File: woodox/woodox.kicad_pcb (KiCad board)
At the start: 2 copper layers, 162.2 x 126.5 mm, 0 parts

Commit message: finish left hand pcb
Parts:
- added C10: 1uF, Capacitor_SMD:C_0402_1005Metric, B.Cu at (189.2, 63.3)
- added C11: 1uF, Capacitor_SMD:C_0402_1005Metric, B.Cu at (188.1, 67.5)
- added C12: 10uF, Capacitor_SMD:C_0402_1005Metric, B.Cu at (69.4, 42.3)
- added C13: 0.1uF, Capacitor_SMD:C_0402_1005Metric, B.Cu at (188.8, 68.2)
- added C14: 0.1uF, Capacitor_SMD:C_0402_1005Metric, B.Cu at (183.1, 76.1)
- added C15: 0.1uF, Capacitor_SMD:C_0402_1005Metric, B.Cu at (189.4, 68.8)
- added C16: 0.1uF, Capacitor_SMD:C_0402_1005Metric, B.Cu at (184.1, 76.1)
- added C17: 10uF, Capacitor_SMD:C_0402_1005Metric, B.Cu at (63.8, 37.5)
- added C18: 0.1uF, Capacitor_SMD:C_0402_1005Metric, B.Cu at (185.1, 76.1)
- added C19: 0.1uF, Capacitor_SMD:C_0402_1005Metric, B.Cu at (186.0, 76.1)
- added C20: 0.1uF, Capacitor_SMD:C_0402_1005Metric, B.Cu at (187.0, 76.1)
- added C21: 0.1uF, Capacitor_SMD:C_0402_1005Metric, B.Cu at (188.0, 76.1)
- added C22: 0.1uF, Capacitor_SMD:C_0402_1005Metric, B.Cu at (189.0, 76.1)
- added C23: 1uF, Capacitor_SMD:C_0402_1005Metric, B.Cu at (185.0, 98.5)
- added C24: 0.1uF, Capacitor_SMD:C_0402_1005Metric, B.Cu at (185.7, 97.8)
- added C25: 1uF, Capacitor_SMD:C_0402_1005Metric, B.Cu at (183.7, 99.8)
- added C26: 0.1uF, Capacitor_SMD:C_0402_1005Metric, B.Cu at (184.3, 99.1)
- added C27: 1uF, Capacitor_SMD:C_0402_1005Metric, B.Cu at (182.3, 101.2)
- added C28: 0.1uF, Capacitor_SMD:C_0402_1005Metric, B.Cu at (183.0, 100.5)
- added C7: 0.1uF, Capacitor_SMD:C_0402_1005Metric, B.Cu at (189.2, 72.1)
- added C8: 27pF, Capacitor_SMD:C_0402_1005Metric, B.Cu at (174.8, 64.4)
- added C9: 27pF, Capacitor_SMD:C_0402_1005Metric, B.Cu at (174.8, 57.1)
- added D33: LED_RGB, marbastlib-mx:LED_MX_6028R, B.Cu at (65.3, 49.1)
- added D34: LED_RGB, marbastlib-mx:LED_MX_6028R, B.Cu at (65.3, 68.2)
- added D35: LED_RGB, marbastlib-mx:LED_MX_6028R, B.Cu at (65.3, 87.2)
- added D36: LED_RGB, marbastlib-mx:LED_MX_6028R, B.Cu at (65.3, 106.3)
- added D37: LED_RGB, marbastlib-mx:LED_MX_6028R, B.Cu at (67.8, 125.3)
- added D38: LED_RGB, marbastlib-mx:LED_MX_6028R, B.Cu at (86.9, 49.1)
- added D39: LED_RGB, marbastlib-mx:LED_MX_6028R, B.Cu at (86.9, 68.2)
- added D40: LED_RGB, marbastlib-mx:LED_MX_6028R, B.Cu at (86.9, 87.2)
- added D41: LED_RGB, marbastlib-mx:LED_MX_6028R, B.Cu at (86.9, 106.3)
- added D42: LED_RGB, marbastlib-mx:LED_MX_6028R, B.Cu at (105.9, 44.7)
- added D43: LED_RGB, marbastlib-mx:LED_MX_6028R, B.Cu at (105.9, 63.7)
- added D44: LED_RGB, marbastlib-mx:LED_MX_6028R, B.Cu at (105.9, 82.8)
- added D45: LED_RGB, marbastlib-mx:LED_MX_6028R, B.Cu at (105.9, 101.8)
- added D46: LED_RGB, marbastlib-mx:LED_MX_6028R, B.Cu at (105.7, 120.9)
- added D47: LED_RGB, marbastlib-mx:LED_MX_6028R, B.Cu at (125.0, 42.1)
- added D48: LED_RGB, marbastlib-mx:LED_MX_6028R, B.Cu at (125.0, 61.2)
- added D49: LED_RGB, marbastlib-mx:LED_MX_6028R, B.Cu at (125.0, 80.2)
- added D50: LED_RGB, marbastlib-mx:LED_MX_6028R, B.Cu at (125.0, 99.3)
- added D51: LED_RGB, marbastlib-mx:LED_MX_6028R, B.Cu at (124.7, 118.3)
- added D52: LED_RGB, marbastlib-mx:LED_MX_6028R, B.Cu at (144.0, 44.7)
- added D53: LED_RGB, marbastlib-mx:LED_MX_6028R, B.Cu at (144.0, 63.7)
- added D54: LED_RGB, marbastlib-mx:LED_MX_6028R, B.Cu at (144.0, 82.8)
- added D55: LED_RGB, marbastlib-mx:LED_MX_6028R, B.Cu at (144.0, 101.8)
- added D56: LED_RGB, marbastlib-mx:LED_MX_6028R, B.Cu at (151.5, 124.2)
- added D57: LED_RGB, marbastlib-mx:LED_MX_6028R, B.Cu at (163.1, 46.6)
- added D58: LED_RGB, marbastlib-mx:LED_MX_6028R, B.Cu at (163.1, 65.6)
- added D59: LED_RGB, marbastlib-mx:LED_MX_6028R, B.Cu at (163.1, 84.7)
- added D60: LED_RGB, marbastlib-mx:LED_MX_6028R, B.Cu at (163.1, 103.7)
- added D61: LED_RGB, marbastlib-mx:LED_MX_6028R, B.Cu at (188.2, 110.8)
- added D62: LED_RGB, marbastlib-mx:LED_MX_6028R, B.Cu at (169.1, 133.6)
- added D63: LED_RGB, marbastlib-mx:LED_MX_6028R, B.Cu at (204.6, 120.3)
- added D64: LED_RGB, marbastlib-mx:LED_MX_6028R, B.Cu at (185.6, 143.1)
- added IC2: W25Q16JVUXIQ_TR, W25Q16JVUXIQ_TR:SON50P300X200X60-9N, B.Cu at (185.8, 70.9)
- added IC3: IS31FL3741A-QFLS4-TR, IS31FL3741A-QFLS4-TR:QFN40P700X700X80-61N-D, B.Cu at (182.9, 91.4)
- added J2: Conn_01x03_Female, Connector_PinHeader_2.54mm:PinHeader_1x03_P2.54mm_Vertical, B.Cu at (87.9, 39.3)
- added J3: USB_C_Receptacle, Connector_USB:USB_C_Receptacle_Amphenol_12401610E4-2A, B.Cu at (76.2, 40.6)
- added J4: Interconnect Left, Connector_USB:USB_C_Receptacle_Amphenol_12401610E4-2A, B.Cu at (184.0, 43.5)
- added R19: 1k, Resistor_SMD:R_0603_1608Metric, B.Cu at (176.0, 41.5)
- added R20: 10k, Resistor_SMD:R_0603_1608Metric, B.Cu at (187.2, 73.3)
- added R21: 27.4, Resistor_SMD:R_0603_1608Metric, B.Cu at (188.0, 57.6)
- added R22: 27.4, Resistor_SMD:R_0603_1608Metric, B.Cu at (189.5, 57.6)
- added R23: 5k1, Resistor_SMD:R_0603_1608Metric, B.Cu at (82.4, 42.9)
- added R24: 5k1, Resistor_SMD:R_0603_1608Metric, B.Cu at (84.0, 42.9)
- added R25: 20, Resistor_SMD:R_0603_1608Metric, B.Cu at (172.3, 95.4)
- added R26: 51, Resistor_SMD:R_0603_1608Metric, B.Cu at (174.0, 88.3)
- added R27: 20, Resistor_SMD:R_0603_1608Metric, B.Cu at (175.1, 87.3)
- added R28: 20, Resistor_SMD:R_0603_1608Metric, B.Cu at (172.9, 89.4)
- added R29: 51, Resistor_SMD:R_0603_1608Metric, B.Cu at (177.2, 85.1)
- added R30: 20, Resistor_SMD:R_0603_1608Metric, B.Cu at (178.3, 84.1)
- added R31: 20, Resistor_SMD:R_0603_1608Metric, B.Cu at (176.1, 86.2)
- added R32: 51, Resistor_SMD:R_0603_1608Metric, B.Cu at (180.4, 81.9)
- added R33: 20, Resistor_SMD:R_0603_1608Metric, B.Cu at (181.5, 80.8)
- added R34: 20, Resistor_SMD:R_0603_1608Metric, B.Cu at (179.3, 83.0)
- added R35: 20, Resistor_SMD:R_0603_1608Metric, B.Cu at (171.9, 90.5)
- added R36: 51, Resistor_SMD:R_0603_1608Metric, B.Cu at (171.2, 94.3)
- added R37: 20, Resistor_SMD:R_0603_1608Metric, B.Cu at (175.5, 98.6)
- added R38: 20, Resistor_SMD:R_0603_1608Metric, B.Cu at (173.3, 96.5)
- added R39: 51, Resistor_SMD:R_0603_1608Metric, B.Cu at (174.4, 97.5)
- added R40: 2k, Resistor_SMD:R_0603_1608Metric, B.Cu at (188.1, 95.8)
- added R41: 2k, Resistor_SMD:R_0603_1608Metric, B.Cu at (187.0, 96.9)
- added R42: 10k, Resistor_SMD:R_0603_1608Metric, B.Cu at (186.3, 99.7)
- added R43: 1k, Resistor_SMD:R_0603_1608Metric, B.Cu at (164.9, 43.8)
- added R44: 1k, Resistor_SMD:R_0603_1608Metric, B.Cu at (174.2, 66.5)
- added SW1: BOOT, Button_Switch_SMD:SW_Push_1P1T_NO_6x6mm_H9.5mm, B.Cu at (170.2, 39.7)
- added SW2: RESET, Button_Switch_SMD:SW_Push_1P1T_NO_6x6mm_H9.5mm, B.Cu at (160.1, 39.7)
- added U35: DRV5057A3, lib:DRV5057A3_K, B.Cu at (65.3, 54.2)
- added U36: DRV5057A3, lib:DRV5057A3_K, B.Cu at (65.3, 73.2)
- added U37: DRV5057A3, lib:DRV5057A3_K, B.Cu at (65.3, 92.3)
- added U38: DRV5057A3, lib:DRV5057A3_K, B.Cu at (65.3, 111.3)
- added U39: DRV5057A3, lib:DRV5057A3_K, B.Cu at (67.8, 130.4)
- added U40: DRV5057A3, lib:DRV5057A3_K, B.Cu at (86.9, 54.2)
- added U41: DRV5057A3, lib:DRV5057A3_K, B.Cu at (86.9, 73.2)
- added U42: DRV5057A3, lib:DRV5057A3_K, B.Cu at (86.9, 92.3)
- added U43: DRV5057A3, lib:DRV5057A3_K, B.Cu at (86.9, 111.3)
- added U44: CD74HC4067M, Package_SO:SOIC-24W_7.5x15.4mm_P1.27mm, B.Cu at (94.0, 127.0)
- added U45: DRV5057A3, lib:DRV5057A3_K, B.Cu at (105.9, 49.8)
- added U46: DRV5057A3, lib:DRV5057A3_K, B.Cu at (105.9, 68.8)
- added U47: DRV5057A3, lib:DRV5057A3_K, B.Cu at (105.9, 87.9)
- added U48: DRV5057A3, lib:DRV5057A3_K, B.Cu at (105.9, 106.9)
- added U49: DRV5057A3, lib:DRV5057A3_K, B.Cu at (105.7, 126.0)
- added U50: CD74HC4067M, Package_SO:SOIC-24W_7.5x15.4mm_P1.27mm, B.Cu at (152.7, 112.7)
- added U51: DRV5057A3, lib:DRV5057A3_K, B.Cu at (125.0, 47.2)
- added U52: DRV5057A3, lib:DRV5057A3_K, B.Cu at (125.0, 66.3)
- added U53: DRV5057A3, lib:DRV5057A3_K, B.Cu at (125.0, 85.3)
- added U54: DRV5057A3, lib:DRV5057A3_K, B.Cu at (125.0, 104.4)
- added U55: DRV5057A3, lib:DRV5057A3_K, B.Cu at (124.7, 123.4)
- added U56: DRV5057A3, lib:DRV5057A3_K, B.Cu at (144.0, 49.8)
- added U57: DRV5057A3, lib:DRV5057A3_K, B.Cu at (144.0, 68.8)
- added U58: DRV5057A3, lib:DRV5057A3_K, B.Cu at (144.0, 87.9)
- added U59: DRV5057A3, lib:DRV5057A3_K, B.Cu at (144.0, 106.9)
- added U60: DRV5057A3, lib:DRV5057A3_K, B.Cu at (150.2, 129.1)
- added U61: DRV5057A3, lib:DRV5057A3_K, B.Cu at (163.1, 51.7)
- added U62: DRV5057A3, lib:DRV5057A3_K, B.Cu at (163.1, 70.7)
- added U63: DRV5057A3, lib:DRV5057A3_K, B.Cu at (163.1, 89.8)
- added U64: DRV5057A3, lib:DRV5057A3_K, B.Cu at (163.1, 108.8)
- added U65: DRV5057A3, lib:DRV5057A3_K, B.Cu at (185.6, 115.2)
- added U66: DRV5057A3, lib:DRV5057A3_K, B.Cu at (173.5, 136.1)
- added U67: RP2040, Package_DFN_QFN:QFN-56-1EP_7x7mm_P0.4mm_EP3.2x3.2mm, B.Cu at (182.9, 63.5)
- added U68: DRV5057A3, lib:DRV5057A3_K, B.Cu at (202.1, 124.7)
- added U69: DRV5057A3, lib:DRV5057A3_K, B.Cu at (190.0, 145.6)
- added U70: NCP1117-3.3_SOT223, Package_TO_SOT_SMD:SOT-223-3_TabPin2, B.Cu at (64.1, 41.8)
- added Y1: ABLS-12.000MHZ-B4-T, Crystal:Crystal_SMD_5032-2Pin_5.0x3.2mm, B.Cu at (174.8, 60.7)
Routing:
- net +3.3V: track 0.00 -> 915.9 mm, vias 0 -> 34
- net /Left Hand/SW_L_2: track 0.00 -> 273.4 mm, vias 0 -> 2
- net /Left Hand/SW_L_1: track 0.00 -> 261.4 mm, vias 0 -> 2
- net /Left Hand/SW_L_3: track 0.00 -> 257.8 mm, vias 0 -> 2
- net /Left Hand/L_R_4: track 0.00 -> 195.6 mm, vias 0 -> 8
- net /Left Hand/L_R_5: track 0.00 -> 186.3 mm, vias 0 -> 7
- net /Left Hand/SW_L_5: track 0.00 -> 185.3 mm, vias 0 -> 2
- net /Left Hand/L_R_1: track 0.00 -> 181.0 mm, vias 0 -> 8
- net /Left Hand/L_G_4: track 0.00 -> 175.5 mm, vias 0 -> 8
- net /Left Hand/L_B_4: track 0.00 -> 173.5 mm, vias 0 -> 9
- net /Left Hand/L_G_5: track 0.00 -> 166.7 mm, vias 0 -> 7
- net /Left Hand/L_B_1: track 0.00 -> 166.2 mm, vias 0 -> 7
- net /Left Hand/L_G_1: track 0.00 -> 162.4 mm, vias 0 -> 7
- net /Left Hand/L_R_2: track 0.00 -> 161.8 mm, vias 0 -> 8
- net /Left Hand/MUX1 S2: track 0.00 -> 153.9 mm, vias 0 -> 2
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- added copper zone on B.Cu, net GND
- added copper zone on F.Cu, net GND
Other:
- outline, holes or cut-outs redrawn

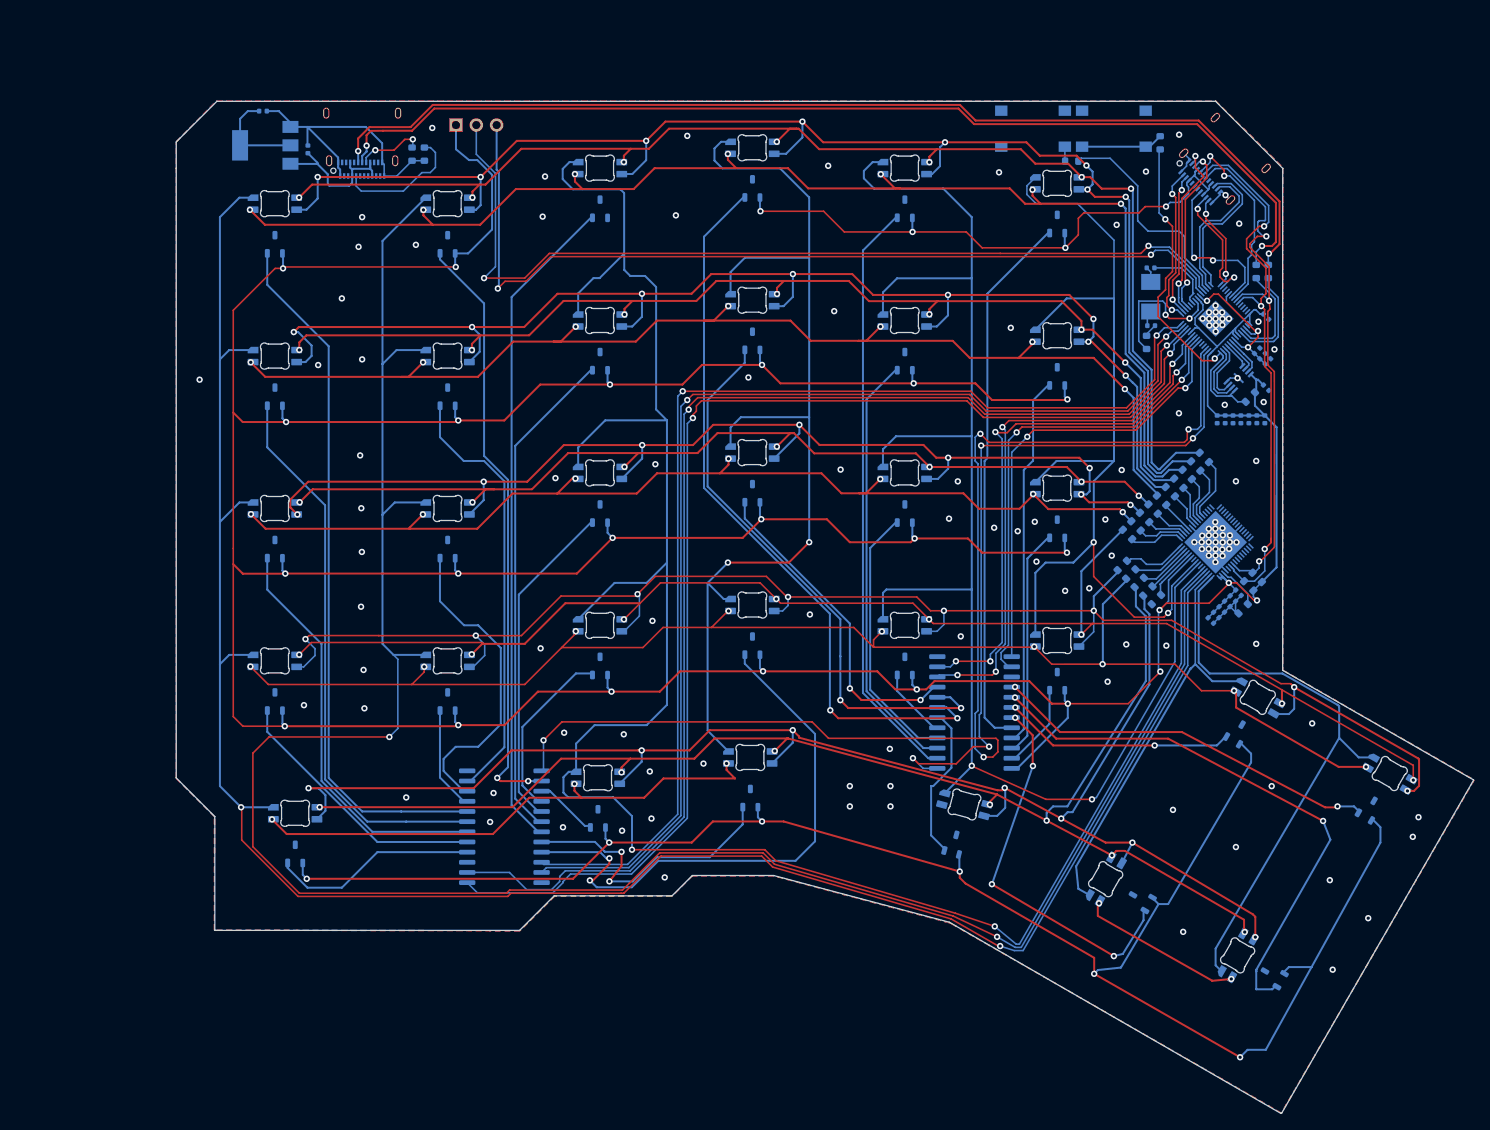
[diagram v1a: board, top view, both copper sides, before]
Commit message: redox woodox left hand pcb
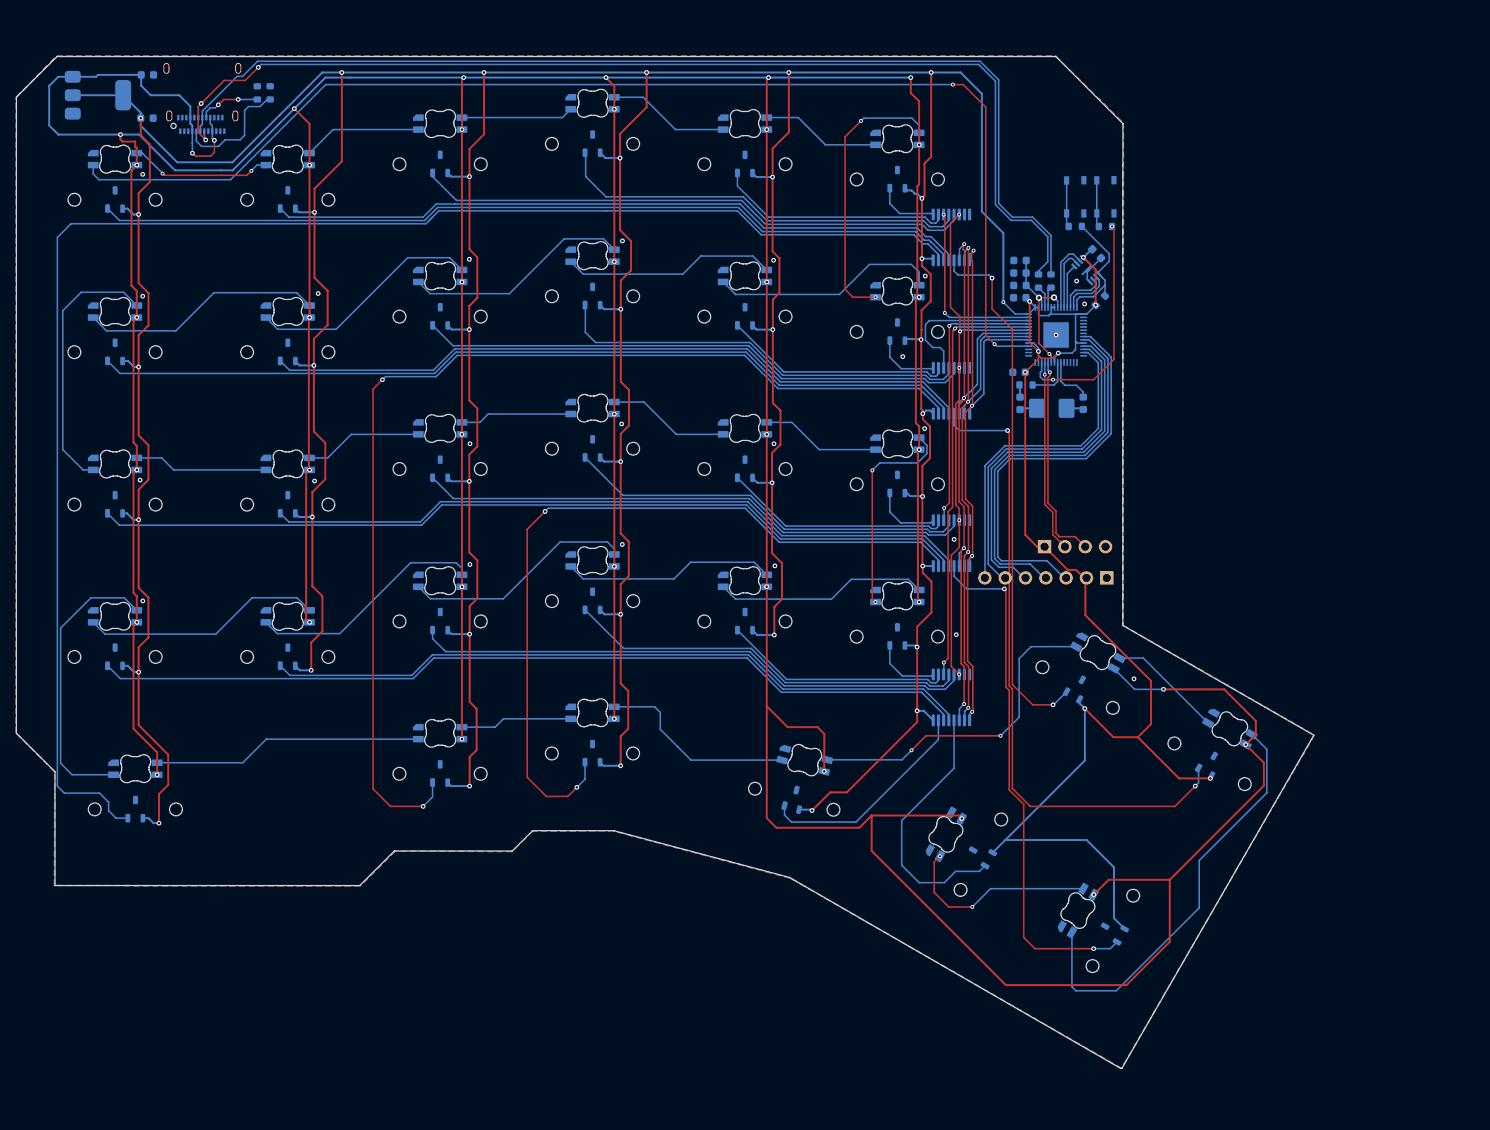
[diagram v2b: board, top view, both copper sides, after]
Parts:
- removed C11, C23, C25, C27: 1uF, Capacitor_SMD:C_0402_1005Metric
- removed C12, C17: 10uF, Capacitor_SMD:C_0402_1005Metric
- removed C13, C14, C15, C16, C18, C19, C20, C21, C22, C24, C26, C28: 0.1uF, Capacitor_SMD:C_0402_1005Metric
- removed D33, D34, D35, D36, D37, D38, D39, D40, D41, D42, D43, D44, D45, D46, D47, D48, D49, D50, D51, D52, D53, D54, D55, D56, D57, D58, D59, D60, D61, D62, D63, D64: LED_RGB, marbastlib-mx:LED_MX_6028R
- removed IC2: W25Q16JVUXIQ_TR, W25Q16JVUXIQ_TR:SON50P300X200X60-9N
- removed IC3: IS31FL3741A-QFLS4-TR, IS31FL3741A-QFLS4-TR:QFN40P700X700X80-61N-D
- removed J3: USB_C_Receptacle, Connector_USB:USB_C_Receptacle_Amphenol_12401610E4-2A
- removed J4: Interconnect Left, Connector_USB:USB_C_Receptacle_Amphenol_12401610E4-2A
- removed R19, R43, R44: 1k, Resistor_SMD:R_0603_1608Metric
- removed R20, R42: 10k, Resistor_SMD:R_0603_1608Metric
- removed R21, R22: 27.4, Resistor_SMD:R_0603_1608Metric
- removed R23, R24: 5k1, Resistor_SMD:R_0603_1608Metric
- removed R25, R27, R28, R30, R31, R33, R34, R35, R37, R38: 20, Resistor_SMD:R_0603_1608Metric
- removed R26, R29, R32, R36, R39: 51, Resistor_SMD:R_0603_1608Metric
- removed R40, R41: 2k, Resistor_SMD:R_0603_1608Metric
- removed U40, U41, U42, U43, U45, U46, U47, U48, U49, U51, U52, U53, U54, U55, U56, U57, U58, U59, U60, U61, U62, U63, U64, U65, U66, U68, U69: DRV5057A3, lib:DRV5057A3_K
- removed U44, U50: CD74HC4067M, Package_SO:SOIC-24W_7.5x15.4mm_P1.27mm
- removed U67: RP2040, Package_DFN_QFN:QFN-56-1EP_7x7mm_P0.4mm_EP3.2x3.2mm
- removed U70: NCP1117-3.3_SOT223, Package_TO_SOT_SMD:SOT-223-3_TabPin2
- added C1: 0.1uF, Capacitor_SMD:C_0603_1608Metric, B.Cu at (168.0, 55.4)
- added C2: 27pF, Capacitor_SMD:C_0603_1608Metric, B.Cu at (158.4, 74.1)
- added C3: 27pF, Capacitor_SMD:C_0603_1608Metric, B.Cu at (166.3, 74.1)
- added C4: 1uF, Capacitor_SMD:C_0603_1608Metric, B.Cu at (158.4, 59.3)
- added C5: 1uF, Capacitor_SMD:C_0603_1608Metric, B.Cu at (158.3, 70.2)
- added C6: 10uF, Capacitor_SMD:C_0603_1608Metric, B.Cu at (49.4, 33.0)
- added IC1: W25Q16JVUXIQ_TR, W25Q16JVUXIQ_TR:SON50P300X200X60-9N, B.Cu at (166.7, 57.4)
- added J1: Conn_01x03_Female, Connector_PinHeader_2.54mm:PinHeader_1x04_P2.54mm_Vertical, B.Cu at (161.5, 92.0)
- added LED1: MX_SK6812MINI-E, lib:LED_MX_SK6812MINI-R, B.Cu at (45.3, 48.6)
- added LED10: MX_SK6812MINI-E, lib:LED_MX_SK6812MINI-R, B.Cu at (85.9, 44.2)
- added LED11: MX_SK6812MINI-E, lib:LED_MX_SK6812MINI-R, B.Cu at (85.9, 63.2)
- added LED12: MX_SK6812MINI-E, lib:LED_MX_SK6812MINI-R, B.Cu at (85.9, 82.3)
- added LED13: MX_SK6812MINI-E, lib:LED_MX_SK6812MINI-R, B.Cu at (85.9, 101.3)
- added LED14: MX_SK6812MINI-E, lib:LED_MX_SK6812MINI-R, B.Cu at (85.9, 120.4)
- added LED15: MX_SK6812MINI-E, lib:LED_MX_SK6812MINI-R, B.Cu at (105.0, 41.6)
- added LED16: MX_SK6812MINI-E, lib:LED_MX_SK6812MINI-R, B.Cu at (105.0, 60.7)
- added LED17: MX_SK6812MINI-E, lib:LED_MX_SK6812MINI-R, B.Cu at (105.0, 79.7)
- added LED18: MX_SK6812MINI-E, lib:LED_MX_SK6812MINI-R, B.Cu at (105.0, 98.8)
- added LED19: MX_SK6812MINI-E, lib:LED_MX_SK6812MINI-R, B.Cu at (105.0, 117.8)
- added LED2: MX_SK6812MINI-E, lib:LED_MX_SK6812MINI-R, B.Cu at (45.3, 67.7)
- added LED20: MX_SK6812MINI-E, lib:LED_MX_SK6812MINI-R, B.Cu at (124.0, 44.2)
- added LED21: MX_SK6812MINI-E, lib:LED_MX_SK6812MINI-R, B.Cu at (124.0, 63.2)
- added LED22: MX_SK6812MINI-E, lib:LED_MX_SK6812MINI-R, B.Cu at (124.0, 82.3)
- added LED23: MX_SK6812MINI-E, lib:LED_MX_SK6812MINI-R, B.Cu at (124.0, 101.3)
- added LED24: MX_SK6812MINI-E, lib:LED_MX_SK6812MINI-R, B.Cu at (130.2, 123.6)
- added LED25: MX_SK6812MINI-E, lib:LED_MX_SK6812MINI-R, B.Cu at (143.1, 46.1)
- added LED26: MX_SK6812MINI-E, lib:LED_MX_SK6812MINI-R, B.Cu at (143.1, 65.1)
- added LED27: MX_SK6812MINI-E, lib:LED_MX_SK6812MINI-R, B.Cu at (143.1, 84.2)
- added LED28: MX_SK6812MINI-E, lib:LED_MX_SK6812MINI-R, B.Cu at (143.1, 103.2)
- added LED29: MX_SK6812MINI-E, lib:LED_MX_SK6812MINI-R, B.Cu at (165.6, 109.6)
- added LED3: MX_SK6812MINI-E, lib:LED_MX_SK6812MINI-R, B.Cu at (45.3, 86.7)
- added LED30: MX_SK6812MINI-E, lib:LED_MX_SK6812MINI-R, B.Cu at (153.5, 130.5)
- added LED31: MX_SK6812MINI-E, lib:LED_MX_SK6812MINI-R, B.Cu at (182.1, 119.1)
- added LED32: MX_SK6812MINI-E, lib:LED_MX_SK6812MINI-R, B.Cu at (170.0, 140.0)
- added LED4: MX_SK6812MINI-E, lib:LED_MX_SK6812MINI-R, B.Cu at (45.3, 105.8)
- added LED5: MX_SK6812MINI-E, lib:LED_MX_SK6812MINI-R, B.Cu at (47.8, 124.8)
- added LED6: MX_SK6812MINI-E, lib:LED_MX_SK6812MINI-R, B.Cu at (66.9, 48.6)
- added LED7: MX_SK6812MINI-E, lib:LED_MX_SK6812MINI-R, B.Cu at (66.9, 67.7)
- added LED8: MX_SK6812MINI-E, lib:LED_MX_SK6812MINI-R, B.Cu at (66.9, 86.7)
- added LED9: MX_SK6812MINI-E, lib:LED_MX_SK6812MINI-R, B.Cu at (66.9, 105.8)
- added R1: 1k, Resistor_SMD:R_0603_1608Metric, B.Cu at (165.3, 52.0)
- added R2: 10k, Resistor_SMD:R_0603_1608Metric, B.Cu at (168.5, 61.2)
- added R3: 1k, Resistor_SMD:R_0603_1608Metric, B.Cu at (159.2, 71.8)
- added R4: 27.4, Resistor_SMD:R_0603_1608Metric, B.Cu at (160.7, 58.8)
- added R5: 27.4, Resistor_SMD:R_0603_1608Metric, B.Cu at (162.3, 58.8)
- added R6: 5k1, Resistor_SMD:R_0603_1608Metric, B.Cu at (63.1, 35.3)
- added R7: 5k1, Resistor_SMD:R_0603_1608Metric, B.Cu at (64.7, 35.3)
- added R8: 1k, Resistor_SMD:R_0603_1608Metric, B.Cu at (169.1, 52.0)
- added U1: DRV5057A3, lib:DRV5057A3_K, B.Cu at (45.3, 48.6)
- added U10: OLED_256x64_I2C, Connector_PinHeader_2.54mm:PinHeader_1x07_P2.54mm_Vertical, B.Cu at (169.3, 95.9)
- added U11: DRV5057A3, lib:DRV5057A3_K, B.Cu at (85.9, 44.2)
- added U12: DRV5057A3, lib:DRV5057A3_K, B.Cu at (85.9, 63.2)
- added U13: DRV5057A3, lib:DRV5057A3_K, B.Cu at (85.9, 82.3)
- added U14: DRV5057A3, lib:DRV5057A3_K, B.Cu at (85.9, 101.3)
- added U15: DRV5057A3, lib:DRV5057A3_K, B.Cu at (85.9, 120.3)
- added U16: DRV5057A3, lib:DRV5057A3_K, B.Cu at (105.0, 41.6)
- added U17: DRV5057A3, lib:DRV5057A3_K, B.Cu at (105.0, 60.7)
- added U18: DRV5057A3, lib:DRV5057A3_K, B.Cu at (105.0, 79.7)
- added U19: DRV5057A3, lib:DRV5057A3_K, B.Cu at (105.0, 98.8)
- added U2: DRV5057A3, lib:DRV5057A3_K, B.Cu at (45.3, 67.6)
- added U20: DRV5057A3, lib:DRV5057A3_K, B.Cu at (105.0, 117.8)
- added U21: DRV5057A3, lib:DRV5057A3_K, B.Cu at (124.0, 44.2)
- added U22: DRV5057A3, lib:DRV5057A3_K, B.Cu at (124.0, 63.2)
- added U23: DRV5057A3, lib:DRV5057A3_K, B.Cu at (124.0, 82.3)
- added U24: DRV5057A3, lib:DRV5057A3_K, B.Cu at (124.0, 101.3)
- added U25: RP2040, Package_DFN_QFN:QFN-56-1EP_7x7mm_P0.4mm_EP3.2x3.2mm, B.Cu at (162.9, 65.5)
- added U26: DRV5057A3, lib:DRV5057A3_K, B.Cu at (130.2, 123.5)
- added U27: DRV5057A3, lib:DRV5057A3_K, B.Cu at (143.1, 46.1)
- added U28: DRV5057A3, lib:DRV5057A3_K, B.Cu at (143.1, 65.1)
- added U29: DRV5057A3, lib:DRV5057A3_K, B.Cu at (143.1, 84.2)
- added U3: DRV5057A3, lib:DRV5057A3_K, B.Cu at (45.3, 86.7)
- added U30: DRV5057A3, lib:DRV5057A3_K, B.Cu at (143.1, 103.2)
- added U31: DRV5057A3, lib:DRV5057A3_K, B.Cu at (165.6, 109.6)
- added U32: DRV5057A3, lib:DRV5057A3_K, B.Cu at (153.6, 130.5)
- added U33: NCP1117-3.3_SOT223, Package_TO_SOT_SMD:SOT-223-3_TabPin2, B.Cu at (43.2, 35.6)
- added U34: 74HC4051, Package_SO:TSSOP-16_4.4x5mm_P0.65mm, B.Cu at (149.9, 53.3)
- added U4: DRV5057A3, lib:DRV5057A3_K, B.Cu at (45.3, 105.7)
- added U5: DRV5057A3, lib:DRV5057A3_K, B.Cu at (47.8, 124.8)
- added U6: DRV5057A3, lib:DRV5057A3_K, B.Cu at (66.9, 48.6)
- added U7: DRV5057A3, lib:DRV5057A3_K, B.Cu at (66.9, 67.6)
- added U8: DRV5057A3, lib:DRV5057A3_K, B.Cu at (66.9, 86.7)
- added U9: DRV5057A3, lib:DRV5057A3_K, B.Cu at (66.9, 105.7)
- C10: value 1uF -> 10uF; footprint Capacitor_SMD:C_0402_1005Metric -> Capacitor_SMD:C_0603_1608Metric
- C7: footprint Capacitor_SMD:C_0402_1005Metric -> Capacitor_SMD:C_0603_1608Metric
- C8: value 27pF -> 1uF; footprint Capacitor_SMD:C_0402_1005Metric -> Capacitor_SMD:C_0603_1608Metric
- C9: value 27pF -> 0.1uF; footprint Capacitor_SMD:C_0402_1005Metric -> Capacitor_SMD:C_0603_1608Metric
- J2: value Conn_01x03_Female -> USB_C_Receptacle; footprint Connector_PinHeader_2.54mm:PinHeader_1x03_P2.54mm_Vertical -> Connector_USB:USB_C_Receptacle_Amphenol_12401610E4-2A
- SW1, SW2: footprint Button_Switch_SMD:SW_Push_1P1T_NO_6x6mm_H9.5mm -> Button_Switch_SMD:SW_Push_1P1T_NO_Vertical_Wuerth_434133025816
- U35, U36, U37: value DRV5057A3 -> 74HC4051; footprint lib:DRV5057A3_K -> Package_SO:TSSOP-16_4.4x5mm_P0.65mm
- Y1: value ABLS-12.000MHZ-B4-T -> ECS-120-8-30-JGN-TR
- moved C10 142.1 mm to (49.3, 38.4), turned to 0 degrees
- moved U38 117.1 mm to (182.1, 119.1), turned to 60 degrees
- moved U39 102.7 mm to (170.1, 140.0), turned to 150 degrees
- moved U37 86.6 mm to (149.9, 110.8), turned to -90 degrees
- moved U35 86.5 mm to (149.9, 72.5), turned to -90 degrees
- moved U36 86.5 mm to (149.9, 91.6), turned to -90 degrees
- moved C7 34.0 mm to (158.4, 57.8), turned to 0 degrees
- moved J2 32.0 mm to (56.2, 35.0), turned to 0 degrees
- moved Y1 18.6 mm to (162.4, 74.7), turned to 0 degrees
- moved C8 16.8 mm to (158.4, 60.9), turned to 180 degrees
- moved C9 16.4 mm to (158.4, 56.2)
- moved SW2 12.4 mm to (169.1, 48.3), turned to 90 degrees
- moved SW1 9.79 mm to (165.3, 48.3), turned to 90 degrees
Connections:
- C7 pad 1: +3.3V -> GND
- C7 pad 2: GND -> Net-(U25-VREG_VOUT)
- C8 pad 1: Net-(C8-Pad1) -> +3.3V
- C8 pad 2: Net-(C8-Pad2) -> GND
- C9 pad 1: Net-(C9-Pad1) -> GND
- C9 pad 2: Net-(C9-Pad2) -> Net-(U25-VREG_VOUT)
- U35 pad 1: +3.3V -> Net-(U28-OUT)
- U35 pad 3: GND -> /MUX2 COM
- U36 pad 1: +3.3V -> Net-(U29-OUT)
- U36 pad 3: GND -> /MUX3 COM
- U37 pad 1: +3.3V -> Net-(U30-OUT)
- U37 pad 3: GND -> /MUX4 COM
- U38 pad 2: Net-(U38-Pad2) -> Net-(U35-A3)
- U39 pad 2: Net-(U39-Pad2) -> Net-(U36-A3)
- Y1 pad 1: Net-(C8-Pad1) -> Net-(C2-Pad1)
- Y1 pad 2: Net-(C9-Pad1) -> Net-(C3-Pad1)
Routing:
- net +5V: track 0.00 -> 781.1 mm, vias 0 -> 40
- net /Left Hand/SW_L_2: track 273.4 -> 0.00 mm, vias 2 -> 0
- net /Left Hand/SW_L_1: track 261.4 -> 0.00 mm, vias 2 -> 0
- net /Left Hand/SW_L_3: track 257.8 -> 0.00 mm, vias 2 -> 0
- net /Left Hand/L_R_4: track 195.6 -> 0.00 mm, vias 8 -> 0
- net Net-(U34-A2): track 0.00 -> 195.0 mm
- net /Left Hand/L_R_5: track 186.3 -> 0.00 mm, vias 7 -> 0
- net /Left Hand/SW_L_5: track 185.3 -> 0.00 mm, vias 2 -> 0
- net /Left Hand/L_R_1: track 181.0 -> 0.00 mm, vias 8 -> 0
- net /Left Hand/L_G_4: track 175.5 -> 0.00 mm, vias 8 -> 0
- net /Left Hand/L_B_4: track 173.5 -> 0.00 mm, vias 9 -> 0
- net /Left Hand/L_G_5: track 166.7 -> 0.00 mm, vias 7 -> 0
- net /Left Hand/L_B_1: track 166.2 -> 0.00 mm, vias 7 -> 0
- net /Left Hand/L_G_1: track 162.4 -> 0.00 mm, vias 7 -> 0
- net /Left Hand/L_R_2: track 161.8 -> 0.00 mm, vias 8 -> 0
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
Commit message: cleanup pcb
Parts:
- U1, U11, U12, U13, U14, U15, U16, U17, U18, U19, U2, U20, U21, U22, U23, U24, U26, U27, U28, U29, U3, U30, U31, U32, U38, U39, U4, U5, U6, U7, U8, U9: footprint lib:DRV5057A3_K -> lib:DRV505x
- U10: footprint Connector_PinHeader_2.54mm:PinHeader_1x07_P2.54mm_Vertical -> lib:OLED_256x64_I2C; moved to F.Cu
- moved U10 33.4 mm to (161.6, 63.4)
- moved LED5 9.50 mm to (57.4, 124.8)
- moved U5 9.50 mm to (57.3, 124.8), turned to 180 degrees
- turned U1 to 180 degrees
- turned U11 to 180 degrees
- turned U12 to 180 degrees
- turned U13 to 180 degrees
- turned U14 to 180 degrees
- turned U15 to 180 degrees
- turned U16 to 180 degrees
- turned U17 to 180 degrees
- turned U18 to 180 degrees
- turned U19 to 180 degrees
- turned U2 to 180 degrees
- turned U20 to 180 degrees
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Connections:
- U25 pad 12: /D_DC -> /D_SDA
- U25 pad 13: /D_CS -> /D_SCL
- U25 pad 8: /D_SCL -> /D_CS
- U25 pad 9: /D_SDA -> /D_DC
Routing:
- net +3.3V: track 935.5 -> 952.1 mm, vias 47 -> 49
- net Net-(U34-A2): track 195.0 -> 206.6 mm
- net /D_SCL: track 50.5 -> 40.0 mm
- net /D_CS: track 40.9 -> 50.9 mm
- net Net-(LED14-DIN): track 33.9 -> 24.4 mm
- net Net-(LED4-DOUT): track 35.8 -> 45.3 mm
- net +5V: track 781.1 -> 789.0 mm
- net /D_DC: track 42.5 -> 48.5 mm
- net /D_SDA: track 47.9 -> 42.4 mm
- net Net-(U35-A3): track 80.7 -> 81.2 mm
